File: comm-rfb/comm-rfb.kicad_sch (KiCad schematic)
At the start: 5 parts, among them J1 PC104_Connector

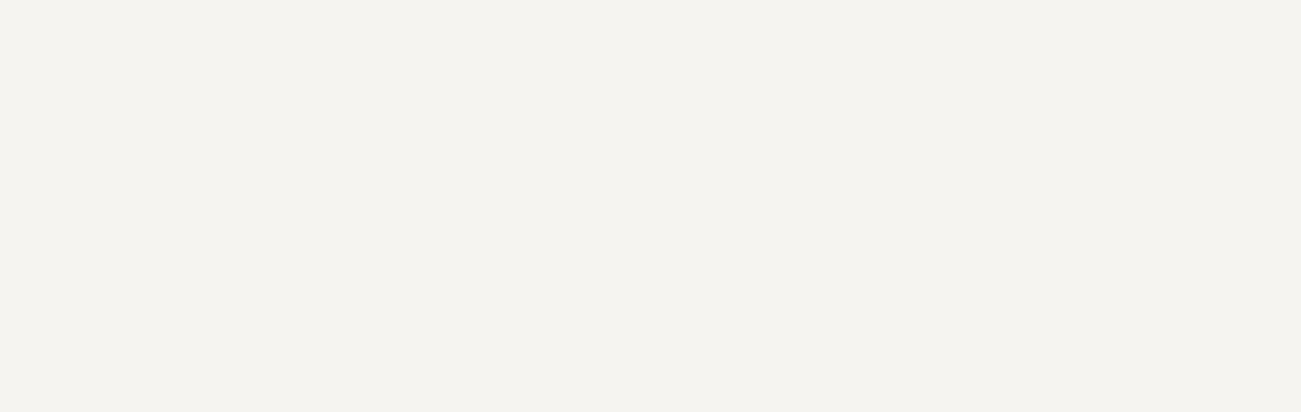
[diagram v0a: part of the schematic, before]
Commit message: schematics of smd - also to test saving
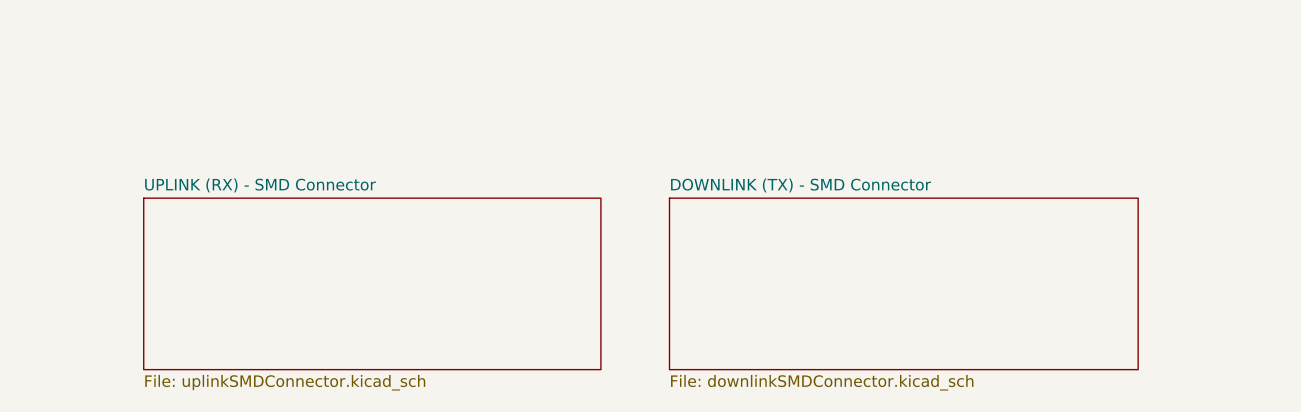
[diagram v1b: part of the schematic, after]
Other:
- added sheet DOWNLINK (TX) - SMD Connector (downlinkSMDConnector.kicad_sch)
- added sheet UPLINK (RX) - SMD Connector (uplinkSMDConnector.kicad_sch)
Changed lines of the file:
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@@
     (pin "1")
+  )
+  (sheet (at 86.36 115.57) (size 52.07 19.05) (fields_autoplaced)
+    (stroke (width 0.1524) (type solid) (color 0 0 0 0))
+    (fill (color 0 0 0 0.0000))
+    (property "Sheet name" "DOWNLINK (TX) - SMD Connector" (id 0) (at 86.36 114.8584 0)
+      (effects (font (size 1.27 1.27)) (justify left bottom))
+    )
+    (property "Sheet file" "downlinkSMDConnector.kicad_sch" (id 1) (at 86.36 135.2046 0)
+      (effects (font (size 1.27 1.27)) (justify left top))
+    )
+  )
+  (sheet (at 27.94 115.57) (size 50.8 19.05) (fields_autoplaced)
+    (stroke (width 0.1524) (type solid) (color 0 0 0 0))
+    (fill (color 0 0 0 0.0000))
+    (property "Sheet name" "UPLINK (RX) - SMD Connector" (id 0) (at 27.94 114.8584 0)
+      (effects (font (size 1.27 1.27)) (justify left bottom))
+    )
+    (property "Sheet file" "uplinkSMDConnector.kicad_sch" (id 1) (at 27.94 135.2046 0)
+      (effects (font (size 1.27 1.27)) (justify left top))
+    )
   )
   (sheet_instances
     (path "/" (page "1"))
+    (path "/75ea27b9-372e-4963-95b4-2f2bcb94e567" (page "2"))
+    (path "/33e637d8-a37e-4c9b-b76e-8d40605182c6" (page "3"))
   )
   (symbol_instances
+    (path "/75ea27b9-372e-4963-95b4-2f2bcb94e567/26a71890-2d50-44c9-938d-65f80d0b6553"
+      (reference "#PWR?") (unit 1) (value "GND") (footprint "")
+    )
+    (path "/75ea27b9-372e-4963-95b4-2f2bcb94e567/876b7789-ceae-4826-a215-3949cd40a636"
+      (reference "#PWR?") (unit 1) (value "GND") (footprint "")
+    )
+    (path "/33e637d8-a37e-4c9b-b76e-8d40605182c6/aed9d855-c10f-4fa2-a7a9-3232c665e97e"
+      (reference "#PWR?") (unit 1) (value "GND") (footprint "")
+    )
+    (path "/33e637d8-a37e-4c9b-b76e-8d40605182c6/ea33cf72-6549-4163-b5be-a9170e251995"
+      (reference "#PWR?") (unit 1) (value "GND") (footprint "")
+    )
     (path "/62767276-38ba-4eba-99b6-994ad2efc4aa"
       (reference "H1") (unit 1) (value "MountingHole_Pad") (footprint "MountingHole:MountingHole_3.2mm_M3_Pad_TopBottom")
@@
       (reference "J1") (unit 1) (value "PC104_Connector") (footprint "pc104-connector:pc104-connector")
     )
+    (path "/75ea27b9-372e-4963-95b4-2f2bcb94e567/000d2391-c268-4c7f-80be-f475a76f7971"
+      (reference "J?") (unit 1) (value "TFM-110-02-SM-D-A-K-TR") (footprint "SAMTEC_TFM-110-02-SM-D-A-K-TR")
+    )
+    (path "/33e637d8-a37e-4c9b-b76e-8d40605182c6/01feaf8d-680b-4fc5-a727-5003e3cd126b"
+      (reference "J?") (unit 1) (value "TFM-110-02-SM-D-A-K-TR") (footprint "SAMTEC_TFM-110-02-SM-D-A-K-TR")
+    )
+    (path "/75ea27b9-372e-4963-95b4-2f2bcb94e567/a2c994cc-ffa4-4456-ac7d-1924ce8dfac1"
+      (reference "J?") (unit 1) (value "TFM-110-02-SM-D-A-K-TR") (footprint "SAMTEC_TFM-110-02-SM-D-A-K-TR")
+    )
+    (path "/33e637d8-a37e-4c9b-b76e-8d40605182c6/f0b90c53-1b24-4712-91ab-6ddafb8cf0dc"
+      (reference "J?") (unit 1) (value "TFM-110-02-SM-D-A-K-TR") (footprint "SAMTEC_TFM-110-02-SM-D-A-K-TR")
+    )
   )

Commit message: sma schematics
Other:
- added sheet SMA Connections (SMAconnections.kicad_sch)
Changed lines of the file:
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@@
     (pin "1")
+  )
+  (sheet (at 149.86 115.57) (size 50.8 19.05) (fields_autoplaced)
+    (stroke (width 0.1524) (type solid) (color 0 0 0 0))
+    (fill (color 0 0 0 0.0000))
+    (property "Sheet name" "SMA Connections" (id 0) (at 149.86 114.8584 0)
+      (effects (font (size 1.27 1.27)) (justify left bottom))
+    )
+    (property "Sheet file" "SMAconnections.kicad_sch" (id 1) (at 149.86 135.2046 0)
+      (effects (font (size 1.27 1.27)) (justify left top))
+    )
   )
   (sheet (at 86.36 115.57) (size 52.07 19.05) (fields_autoplaced)
@@
     (path "/75ea27b9-372e-4963-95b4-2f2bcb94e567" (page "2"))
     (path "/33e637d8-a37e-4c9b-b76e-8d40605182c6" (page "3"))
+    (path "/1134daf0-036a-4c8a-b49c-c0c69387f2ca" (page "4"))
   )
   (symbol_instances
+    (path "/1134daf0-036a-4c8a-b49c-c0c69387f2ca/04d2379e-e386-407e-a10c-0e005123c66c"
+      (reference "#PWR?") (unit 1) (value "GND") (footprint "")
+    )
     (path "/75ea27b9-372e-4963-95b4-2f2bcb94e567/26a71890-2d50-44c9-938d-65f80d0b6553"
+      (reference "#PWR?") (unit 1) (value "GND") (footprint "")
+    )
+    (path "/1134daf0-036a-4c8a-b49c-c0c69387f2ca/734374f1-a5c0-4ca7-80db-2c8df230d4b1"
+      (reference "#PWR?") (unit 1) (value "GND") (footprint "")
+    )
+    (path "/1134daf0-036a-4c8a-b49c-c0c69387f2ca/7f98bc21-20f2-43d6-8ff2-c9637c6cbb0a"
       (reference "#PWR?") (unit 1) (value "GND") (footprint "")
     )
@@
     )
     (path "/33e637d8-a37e-4c9b-b76e-8d40605182c6/aed9d855-c10f-4fa2-a7a9-3232c665e97e"
+      (reference "#PWR?") (unit 1) (value "GND") (footprint "")
+    )
+    (path "/1134daf0-036a-4c8a-b49c-c0c69387f2ca/b96f5805-3055-42df-9755-2669a6ea9d6e"
       (reference "#PWR?") (unit 1) (value "GND") (footprint "")
     )
@@
       (reference "J?") (unit 1) (value "TFM-110-02-SM-D-A-K-TR") (footprint "SAMTEC_TFM-110-02-SM-D-A-K-TR")
     )
+    (path "/1134daf0-036a-4c8a-b49c-c0c69387f2ca/09df4c29-2554-483c-8f70-7e5ec756dcd5"
+      (reference "J?") (unit 1) (value "Conn_Coaxial") (footprint "Connector_Coaxial:SMA_Amphenol_132134-10_Vertical")
+    )
+    (path "/1134daf0-036a-4c8a-b49c-c0c69387f2ca/48f9d1ea-ce9e-45a5-bd04-a4e73a5279ef"
+      (reference "J?") (unit 1) (value "Conn_Coaxial") (footprint "Connector_Coaxial:SMA_Amphenol_132134-10_Vertical")
+    )
+    (path "/1134daf0-036a-4c8a-b49c-c0c69387f2ca/6347bd5d-e257-41d5-aeea-57d18b44cb55"
+      (reference "J?") (unit 1) (value "Conn_Coaxial") (footprint "Connector_Coaxial:SMA_Amphenol_132134-10_Vertical")
+    )
     (path "/75ea27b9-372e-4963-95b4-2f2bcb94e567/a2c994cc-ffa4-4456-ac7d-1924ce8dfac1"
       (reference "J?") (unit 1) (value "TFM-110-02-SM-D-A-K-TR") (footprint "SAMTEC_TFM-110-02-SM-D-A-K-TR")
     )
+    (path "/1134daf0-036a-4c8a-b49c-c0c69387f2ca/dbe6ea1f-ef57-4213-98f3-ca3f3fe7b093"
+      (reference "J?") (unit 1) (value "Conn_Coaxial") (footprint "Connector_Coaxial:SMA_Amphenol_132134-10_Vertical")
+    )
     (path "/33e637d8-a37e-4c9b-b76e-8d40605182c6/f0b90c53-1b24-4712-91ab-6ddafb8cf0dc"

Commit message: power amp schematic
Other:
- added sheet Power Amp (powerAMP.kicad_sch)
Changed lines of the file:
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@@
+    )
+  )
+  (sheet (at 210.82 115.57) (size 58.42 19.05) (fields_autoplaced)
+    (stroke (width 0.1524) (type solid) (color 0 0 0 0))
+    (fill (color 0 0 0 0.0000))
+    (property "Sheet name" "Power Amp" (id 0) (at 210.82 114.8584 0)
+      (effects (font (size 1.27 1.27)) (justify left bottom))
+    )
+    (property "Sheet file" "powerAMP.kicad_sch" (id 1) (at 210.82 135.2046 0)
+      (effects (font (size 1.27 1.27)) (justify left top))
     )
   )
@@
     (path "/33e637d8-a37e-4c9b-b76e-8d40605182c6" (page "3"))
     (path "/1134daf0-036a-4c8a-b49c-c0c69387f2ca" (page "4"))
+    (path "/692e9f18-86ea-4b4e-8432-aeb1e884c0b2" (page "5"))
   )
   (symbol_instances
@@
       (reference "#PWR?") (unit 1) (value "GND") (footprint "")
     )
+    (path "/692e9f18-86ea-4b4e-8432-aeb1e884c0b2/1891302e-feba-46e9-98e1-ac30fb0faa45"
+      (reference "#PWR?") (unit 1) (value "GND") (footprint "")
+    )
     (path "/75ea27b9-372e-4963-95b4-2f2bcb94e567/26a71890-2d50-44c9-938d-65f80d0b6553"
+      (reference "#PWR?") (unit 1) (value "GND") (footprint "")
+    )
+    (path "/692e9f18-86ea-4b4e-8432-aeb1e884c0b2/3fc1f3ca-0173-43c5-a009-6e81b6f97b1f"
       (reference "#PWR?") (unit 1) (value "GND") (footprint "")
     )
@@
       (reference "#PWR?") (unit 1) (value "GND") (footprint "")
     )
+    (path "/692e9f18-86ea-4b4e-8432-aeb1e884c0b2/85ac7498-c369-4034-9983-58cad7ad0b89"
+      (reference "#PWR?") (unit 1) (value "GND") (footprint "")
+    )
     (path "/75ea27b9-372e-4963-95b4-2f2bcb94e567/876b7789-ceae-4826-a215-3949cd40a636"
+      (reference "#PWR?") (unit 1) (value "GND") (footprint "")
+    )
+    (path "/692e9f18-86ea-4b4e-8432-aeb1e884c0b2/9d27d8d5-dbb3-4420-b13b-4ace19e4b49a"
       (reference "#PWR?") (unit 1) (value "GND") (footprint "")
     )
@@
     (path "/33e637d8-a37e-4c9b-b76e-8d40605182c6/ea33cf72-6549-4163-b5be-a9170e251995"
       (reference "#PWR?") (unit 1) (value "GND") (footprint "")
+    )
+    (path "/692e9f18-86ea-4b4e-8432-aeb1e884c0b2/2364a6a1-f6d4-438b-b7eb-4b2cbe8bad70"
+      (reference "C?") (unit 1) (value "1.8p") (footprint "")
+    )
+    (path "/692e9f18-86ea-4b4e-8432-aeb1e884c0b2/2b4f2a19-5abc-496c-95d5-206b91f31acd"
+      (reference "C?") (unit 1) (value "1000p") (footprint "")
+    )
+    (path "/692e9f18-86ea-4b4e-8432-aeb1e884c0b2/5d87e782-851c-4f5f-bf93-d7123ab1bde8"
+      (reference "C?") (unit 1) (value "10p") (footprint "")
+    )
+    (path "/692e9f18-86ea-4b4e-8432-aeb1e884c0b2/700b9959-af68-408a-a0af-c75f7b4c1202"
+      (reference "C?") (unit 1) (value "20p") (footprint "")
+    )
+    (path "/692e9f18-86ea-4b4e-8432-aeb1e884c0b2/7201dc75-4dd5-46e5-8d99-f9732c11de61"
+      (reference "C?") (unit 1) (value "1000p") (footprint "")
+    )
+    (path "/692e9f18-86ea-4b4e-8432-aeb1e884c0b2/9684af4c-3cb4-4602-8482-2b14e29c15f1"
+      (reference "C?") (unit 1) (value "1000p") (footprint "")
+    )
+    (path "/692e9f18-86ea-4b4e-8432-aeb1e884c0b2/b21d1da4-02c1-4f3f-837f-ad80361babc9"
+      (reference "C?") (unit 1) (value "12n") (footprint "")
+    )
+    (path "/692e9f18-86ea-4b4e-8432-aeb1e884c0b2/cb37d10f-c63d-414c-a231-a60cf028d22e"
+      (reference "C?") (unit 1) (value "10p") (footprint "")
     )
     (path "/62767276-38ba-4eba-99b6-994ad2efc4aa"
@@
       (reference "J?") (unit 1) (value "TFM-110-02-SM-D-A-K-TR") (footprint "SAMTEC_TFM-110-02-SM-D-A-K-TR")
     )
+    (path "/692e9f18-86ea-4b4e-8432-aeb1e884c0b2/6000ebf2-7bdc-417f-9120-c9e29b6ff8d2"
+      (reference "L?") (unit 1) (value "150n") (footprint "")
+    )
+    (path "/692e9f18-86ea-4b4e-8432-aeb1e884c0b2/85a53857-7cc3-4f0b-9d07-e8827298a297"
+      (reference "L?") (unit 1) (value "22n") (footprint "")
+    )
+    (path "/692e9f18-86ea-4b4e-8432-aeb1e884c0b2/82515fb1-9eff-4a38-b8b7-126750192eb5"
+      (reference "R?") (unit 1) (value "15") (footprint "")
+    )
+    (path "/692e9f18-86ea-4b4e-8432-aeb1e884c0b2/8387a290-ddef-4d50-bca9-f806c6f0a85f"
+      (reference "R?") (unit 1) (value "330") (footprint "")
+    )
+    (path "/692e9f18-86ea-4b4e-8432-aeb1e884c0b2/bae6c4e0-014f-4b31-94e4-7d32639e5820"
+      (reference "R?") (unit 1) (value "9.1k") (footprint "")
+    )
+    (path "/692e9f18-86ea-4b4e-8432-aeb1e884c0b2/c90ac0f1-4a37-4b59-9cdb-77baf606bb78"
+      (reference "U?") (unit 1) (value "SKY67150-396LF") (footprint "SON50P200X200X80-9N")
+    )
   )

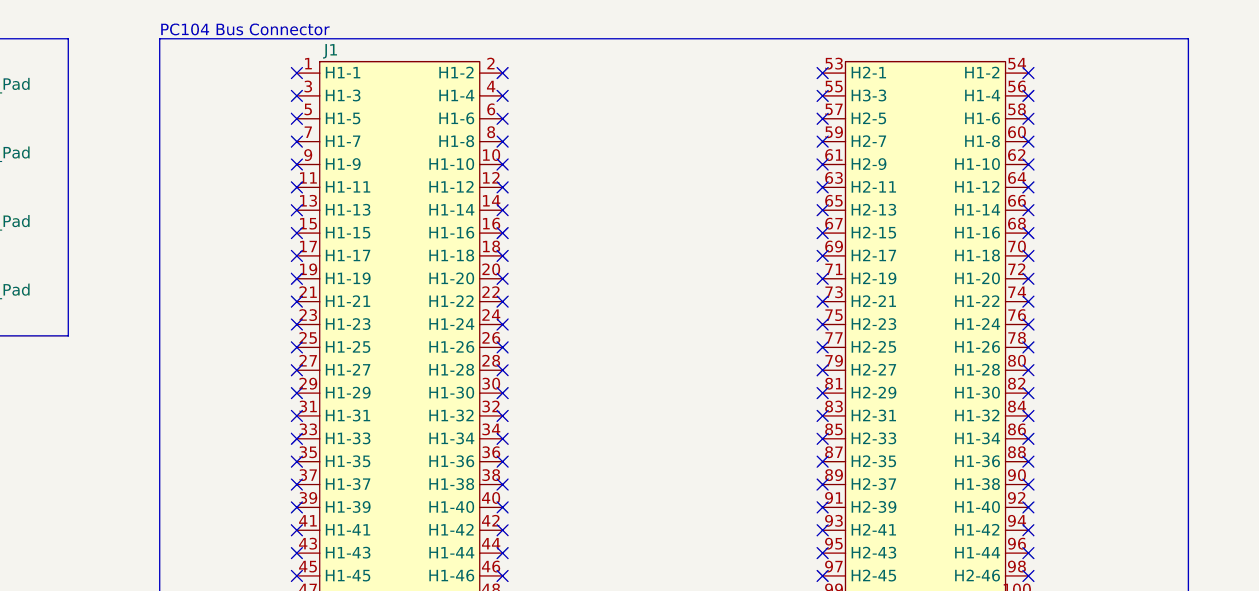
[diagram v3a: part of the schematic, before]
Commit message: pc104 connections schem
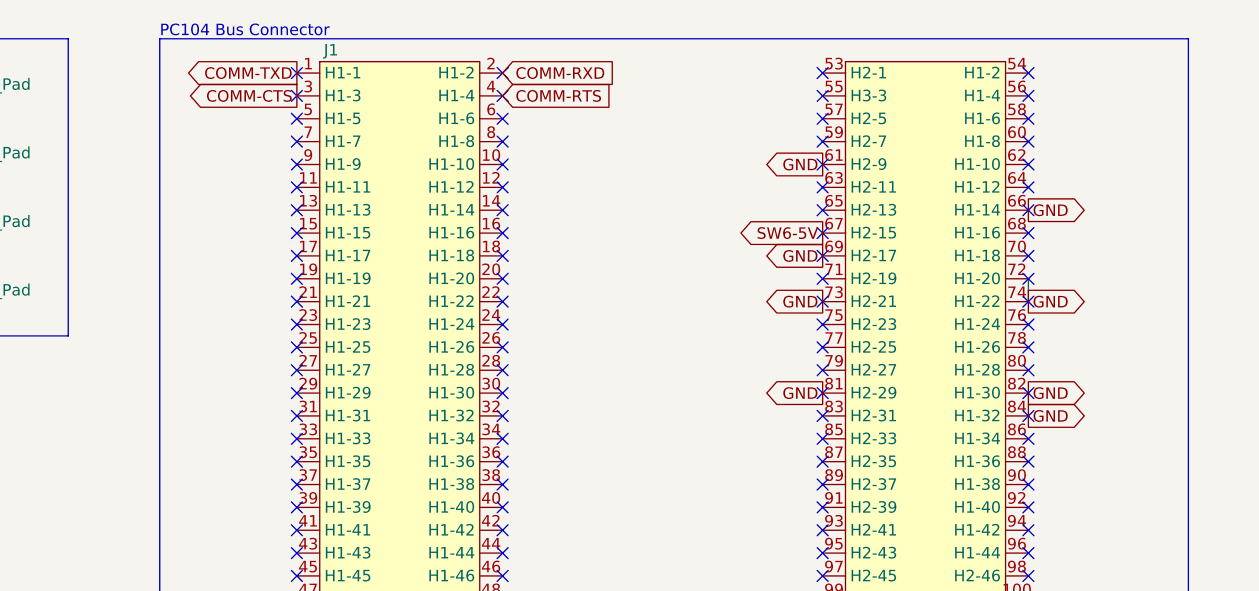
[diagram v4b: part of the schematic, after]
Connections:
- net COMM-TXD: now reaches J1.1 (H1-1)
- net COMM-RXD: now reaches J1.2 (H1-2)
- net COMM-CTS: now reaches J1.3 (H1-3)
- net COMM-RTS: now reaches J1.4 (H1-4)
- net GND: now reaches J1.61 (H2-9)
- net GND: now also J1.66 (H1-14), J1.69 (H2-17), J1.72 (H1-20), J1.73 (H2-21), J1.74 (H1-22), J1.81 (H2-29), J1.82 (H1-30), J1.84 (H1-32)
- net SW6-5V: now reaches J1.67 (H2-15)
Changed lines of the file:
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@@
+    (stroke (width 0) (type default) (color 0 0 0 0))
+  )
+  (wire (pts (xy 147.32 44.45) (xy 147.32 41.91))
     (stroke (width 0) (type default) (color 0 0 0 0))
   )
@@
     (effects (font (size 1.27 1.27)) (justify left bottom))
   )
+  (global_label "GND" (shape output) (at 124.46 39.37 180) (fields_autoplaced)
+    (effects (font (size 1.27 1.27)) (justify right))
+    (property "Intersheet References" "${INTERSHEET_REFS}" (id 0) (at 118.1764 39.2906 0)
+      (effects (font (size 1.27 1.27)) (justify right) hide)
+    )
+  )
+  (global_label "GND" (shape output) (at 147.32 44.45 0) (fields_autoplaced)
+    (effects (font (size 1.27 1.27)) (justify left))
+    (property "Intersheet References" "${INTERSHEET_REFS}" (id 0) (at 153.6036 44.5294 0)
+      (effects (font (size 1.27 1.27)) (justify left) hide)
+    )
+  )
+  (global_label "COMM-RTS" (shape input) (at 88.9 21.59 0) (fields_autoplaced)
+    (effects (font (size 1.27 1.27)) (justify left))
+    (property "Intersheet References" "${INTERSHEET_REFS}" (id 0) (at 101.836 21.5106 0)
+      (effects (font (size 1.27 1.27)) (justify left) hide)
+    )
+  )
+  (global_label "GND" (shape output) (at 147.32 34.29 0) (fields_autoplaced)
+    (effects (font (size 1.27 1.27)) (justify left))
+    (property "Intersheet References" "${INTERSHEET_REFS}" (id 0) (at 153.6036 34.3694 0)
+      (effects (font (size 1.27 1.27)) (justify left) hide)
+    )
+  )
+  (global_label "GND" (shape output) (at 147.32 54.61 0) (fields_autoplaced)
+    (effects (font (size 1.27 1.27)) (justify left))
+    (property "Intersheet References" "${INTERSHEET_REFS}" (id 0) (at 153.6036 54.6894 0)
+      (effects (font (size 1.27 1.27)) (justify left) hide)
+    )
+  )
+  (global_label "SW6-5V" (shape output) (at 124.46 36.83 180) (fields_autoplaced)
+    (effects (font (size 1.27 1.27)) (justify right))
+    (property "Intersheet References" "${INTERSHEET_REFS}" (id 0) (at 114.3059 36.7506 0)
+      (effects (font (size 1.27 1.27)) (justify right) hide)
+    )
+  )
+  (global_label "GND" (shape output) (at 147.32 57.15 0) (fields_autoplaced)
+    (effects (font (size 1.27 1.27)) (justify left))
+    (property "Intersheet References" "${INTERSHEET_REFS}" (id 0) (at 153.6036 57.2294 0)
+      (effects (font (size 1.27 1.27)) (justify left) hide)
+    )
+  )
+  (global_label "GND" (shape output) (at 124.46 54.61 180) (fields_autoplaced)
+    (effects (font (size 1.27 1.27)) (justify right))
+    (property "Intersheet References" "${INTERSHEET_REFS}" (id 0) (at 118.1764 54.5306 0)
+      (effects (font (size 1.27 1.27)) (justify right) hide)
+    )
+  )
+  (global_label "GND" (shape output) (at 124.46 29.21 180) (fields_autoplaced)
+    (effects (font (size 1.27 1.27)) (justify right))
+    (property "Intersheet References" "${INTERSHEET_REFS}" (id 0) (at 118.1764 29.1306 0)
+      (effects (font (size 1.27 1.27)) (justify right) hide)
+    )
+  )
+  (global_label "COMM-TXD" (shape output) (at 66.04 19.05 180) (fields_autoplaced)
+    (effects (font (size 1.27 1.27)) (justify right))
+    (property "Intersheet References" "${INTERSHEET_REFS}" (id 0) (at 53.104 18.9706 0)
+      (effects (font (size 1.27 1.27)) (justify right) hide)
+    )
+  )
+  (global_label "COMM-CTS" (shape output) (at 66.04 21.59 180) (fields_autoplaced)
+    (effects (font (size 1.27 1.27)) (justify right))
+    (property "Intersheet References" "${INTERSHEET_REFS}" (id 0) (at 53.104 21.5106 0)
+      (effects (font (size 1.27 1.27)) (justify right) hide)
+    )
+  )
+  (global_label "COMM-RXD" (shape input) (at 88.9 19.05 0) (fields_autoplaced)
+    (effects (font (size 1.27 1.27)) (justify left))
+    (property "Intersheet References" "${INTERSHEET_REFS}" (id 0) (at 102.1383 18.9706 0)
+      (effects (font (size 1.27 1.27)) (justify left) hide)
+    )
+  )
+  (global_label "GND" (shape output) (at 124.46 44.45 180) (fields_autoplaced)
+    (effects (font (size 1.27 1.27)) (justify right))
+    (property "Intersheet References" "${INTERSHEET_REFS}" (id 0) (at 118.1764 44.3706 0)
+      (effects (font (size 1.27 1.27)) (justify right) hide)
+    )
+  )
   (symbol (lib_id "Mechanical:MountingHole_Pad") (at 17.78 27.94 0) (unit 1)
